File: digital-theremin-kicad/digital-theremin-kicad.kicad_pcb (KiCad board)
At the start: 2 copper layers, 99.1 x 91.1 mm, 40 parts, among them J1 PICO_DDS, J10 R_SPEAKER, J11 L_SPEAKER, J2 VL53L0X-VOL, J3 VL53L0X-FREQ, J4 ToDaughter1, J5 ToDaughter2, J6 Daughter1, J7 DISPLAY, J8 Daughter2, J9 PAM8403 module, SW1 SW_Push, SW2 SW_Push

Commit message: fixes for the digital circuit
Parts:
- moved J7 22.0 mm to (149.9, 123.1)
- moved R3 6.88 mm to (170.0, 91.0)
- moved H2 3.17 mm to (123.2, 140.3)
- moved H2 3.17 mm to (184.2, 140.3)
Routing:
- net +3V3: track 95.4 -> 114.7 mm
- net Net-(J6-Pin_3): track 30.4 -> 16.4 mm
- net GND: track 141.8 -> 132.1 mm
- net Net-(D1-A): track 11.8 -> 5.80 mm
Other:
- board size 99.1 x 91.1 mm -> 99.1 x 87.9 mm
- board text added: "3V3, GND, SCL, SDA"
- board text added: "Balaskó Tímea, Bodnár István, Borbély Sára, Briczky Balázs, Lajtos Hanna, Rácz Réka"
- board text removed: "Balaskó Tímea, Bodnár István, Borbély Sára, Bricky Balázs, Lajtos Hanna, Rácz Réka"

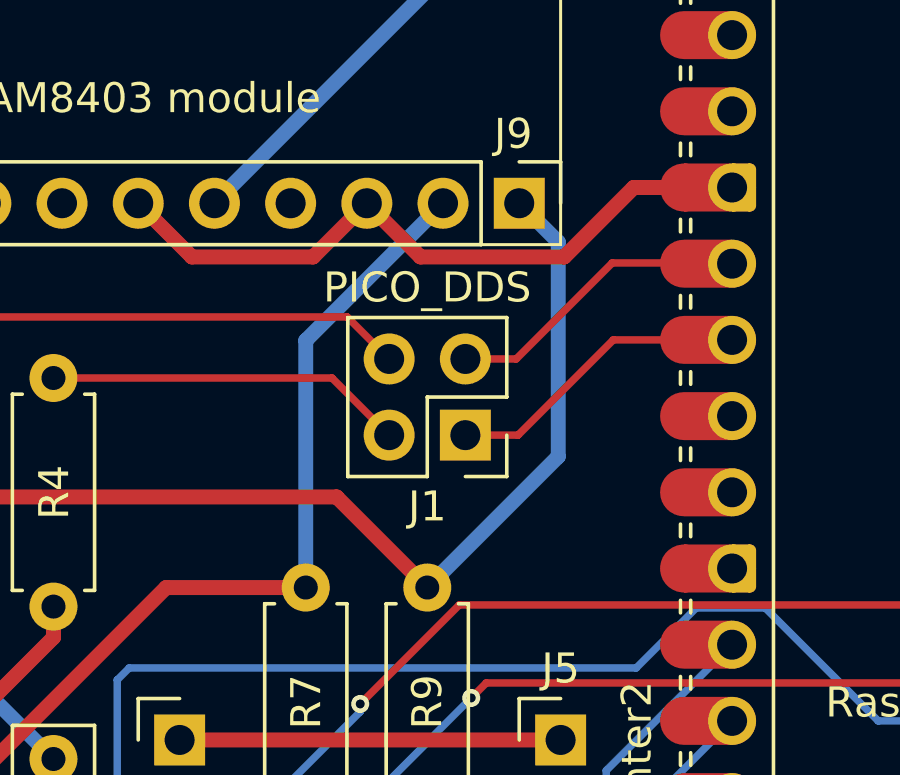
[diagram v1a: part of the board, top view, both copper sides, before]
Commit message: code for the digital theremin
- code is added for digital theremin
- minor fixes for the pcb
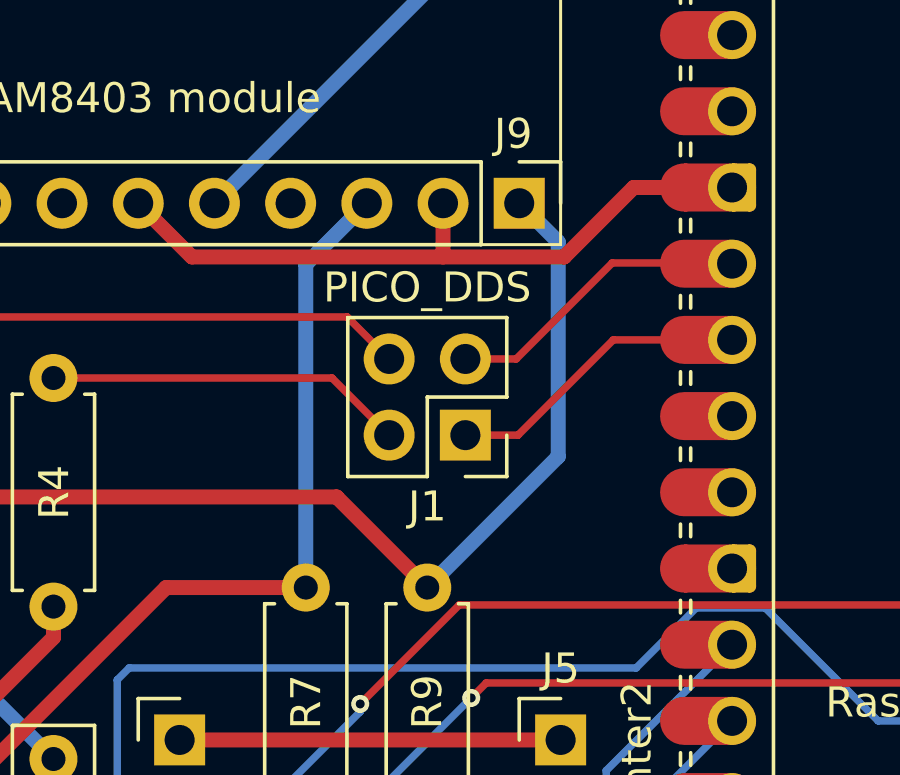
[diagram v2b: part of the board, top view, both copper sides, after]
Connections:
- J9 pad 2: Net-(J9-Pin_2) -> GND
- J9 pad 3: GND -> Net-(J9-Pin_3)
- R10 pad 2: Net-(J9-Pin_2) -> Net-(J9-Pin_3)
- R6 pad 2: Net-(J9-Pin_2) -> Net-(J9-Pin_3)
- R7 pad 2: Net-(J9-Pin_2) -> Net-(J9-Pin_3)
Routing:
- net Net-(J9-Pin_2): track 43.6 -> 0.00 mm
- net Net-(J9-Pin_3): track 0.00 -> 42.6 mm
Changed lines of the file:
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@@
 	(net 57 "Net-(C2-Pad1)")
 	(net 58 "Net-(C3-Pad1)")
-	(net 59 "Net-(J9-Pin_2)")
+	(net 59 "Net-(J9-Pin_3)")
 	(net 60 "Net-(J11-Pin_2)")
 	(footprint "LED_THT:LED_D5.0mm"
@@
 			(layers "*.Cu" "*.Mask")
 			(remove_unused_layers no)
-			(net 59 "Net-(J9-Pin_2)")
+			(net 59 "Net-(J9-Pin_3)")
 			(pintype "passive")
 		)
@@
 			(layers "*.Cu" "*.Mask")
 			(remove_unused_layers no)
-			(net 59 "Net-(J9-Pin_2)")
+			(net 3 "GND")
 			(pinfunction "Pin_2")
 			(pintype "passive")
@@
 			(layers "*.Cu" "*.Mask")
 			(remove_unused_layers no)
-			(net 3 "GND")
+			(net 59 "Net-(J9-Pin_3)")
 			(pinfunction "Pin_3")
 			(pintype "passive")
@@
 			(layers "*.Cu" "*.Mask")
 			(remove_unused_layers no)
-			(net 59 "Net-(J9-Pin_2)")
+			(net 59 "Net-(J9-Pin_3)")
 			(pintype "passive")
 		)
@@
 			(layers "*.Cu" "*.Mask")
 			(remove_unused_layers no)
-			(net 59 "Net-(J9-Pin_2)")
+			(net 59 "Net-(J9-Pin_3)")
 			(pintype "passive")
 		)
@@
 	)
 	(segment
+		(start 141.515 78.185)
+		(end 139.2 80.5)
+		(width 0.5)
+		(layer "F.Cu")
+		(net 3)
+	)
+	(segment
 		(start 122.175 102.235)
 		(end 118.125 102.235)
@@
 	)
 	(segment
+		(start 125 78.71)
+		(end 126.79 80.5)
+		(width 0.5)
+		(layer "F.Cu")
+		(net 3)
+	)
+	(segment
 		(start 139.08 99.14)
 		(end 143.525 103.585)
@@
 	)
 	(segment
-		(start 139.2 80.5)
-		(end 141.515 78.185)
-		(width 0.5)
-		(layer "F.Cu")
-		(net 3)
-	)
-	(segment
 		(start 165.9 102.85)
 		(end 165.165 103.585)
@@
 	)
 	(segment
-		(start 134.41 80.5)
+		(start 126.79 80.5)
 		(end 139.2 80.5)
 		(width 0.5)
@@
 	)
 	(segment
-		(start 126.79 80.5)
-		(end 130.83 80.5)
-		(width 0.5)
-		(layer "F.Cu")
-		(net 3)
-	)
-	(segment
-		(start 125 78.71)
-		(end 126.79 80.5)
-		(width 0.5)
-		(layer "F.Cu")
-		(net 3)
-	)
-	(segment
 		(start 168.29 99.14)
 		(end 168.16 99.14)
@@
 	)
 	(segment
-		(start 132.62 78.71)
-		(end 134.41 80.5)
-		(width 0.5)
-		(layer "F.Cu")
-		(net 3)
-	)
-	(segment
-		(start 130.83 80.5)
-		(end 132.62 78.71)
+		(start 125.27 99.14)
+		(end 122.175 102.235)
 		(width 0.5)
 		(layer "F.Cu")
@@
 	)
 	(segment
-		(start 125.27 99.14)
-		(end 122.175 102.235)
+		(start 143.995 78.185)
+		(end 141.515 78.185)
 		(width 0.5)
 		(layer "F.Cu")
@@
 	)
 	(segment
-		(start 141.515 78.185)
-		(end 143.995 78.185)
+		(start 165.165 103.585)
+		(end 163.375 103.585)
 		(width 0.5)
 		(layer "F.Cu")
@@
 	)
 	(segment
-		(start 165.165 103.585)
-		(end 163.375 103.585)
+		(start 135.16 80.5)
+		(end 135.16 78.71)
 		(width 0.5)
 		(layer "F.Cu")
@@
 	)
 	(segment
-		(start 130.585 83.285)
-		(end 135.16 78.71)
+		(start 130.585 91.52)
+		(end 130.585 80.745)
 		(width 0.5)
 		(layer "B.Cu")
@@
 	)
 	(segment
-		(start 130.585 91.52)
-		(end 130.585 83.285)
+		(start 130.585 80.745)
+		(end 132.62 78.71)
 		(width 0.5)
 		(layer "B.Cu")

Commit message: minor update to the pcb
minor update to the pcb
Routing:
- net +3V3: track 114.7 -> 191.7 mm
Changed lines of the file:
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@@
+	)
+	(segment
+		(start 124.46 97.028)
+		(end 124.46 97.79)
+		(width 0.5)
+		(layer "F.Cu")
+		(net 16)
+	)
+	(segment
+		(start 123.223 111.285)
+		(end 171.385 111.285)
+		(width 0.5)
+		(layer "F.Cu")
+		(net 16)
 	)
 	(segment
@@
 	)
 	(segment
+		(start 126.38 96.6)
+		(end 124.888 96.6)
+		(width 0.5)
+		(layer "F.Cu")
+		(net 16)
+	)
+	(segment
 		(start 168.29 92.71)
 		(end 168.29 96.6)
+		(width 0.5)
+		(layer "F.Cu")
+		(net 16)
+	)
+	(segment
+		(start 124.46 97.79)
+		(end 121.666 100.584)
 		(width 0.5)
 		(layer "F.Cu")
@@
 	)
 	(segment
+		(start 117.348 100.584)
+		(end 116.332 101.6)
+		(width 0.5)
+		(layer "F.Cu")
+		(net 16)
+	)
+	(segment
 		(start 182.41 96.6)
 		(end 186.5 100.69)
@@
 	)
 	(segment
+		(start 116.332 101.6)
+		(end 116.332 104.394)
+		(width 0.5)
+		(layer "F.Cu")
+		(net 16)
+	)
+	(segment
 		(start 126.38 96.6)
 		(end 139.08 96.6)
+		(width 0.5)
+		(layer "F.Cu")
+		(net 16)
+	)
+	(segment
+		(start 171.385 111.285)
+		(end 174.005 108.665)
+		(width 0.5)
+		(layer "F.Cu")
+		(net 16)
+	)
+	(segment
+		(start 116.332 104.394)
+		(end 123.223 111.285)
 		(width 0.5)
 		(layer "F.Cu")
@@
 	)
 	(segment
+		(start 124.888 96.6)
+		(end 124.46 97.028)
+		(width 0.5)
+		(layer "F.Cu")
+		(net 16)
+	)
+	(segment
 		(start 175.39 91)
 		(end 180.99 96.6)
 		(width 0.5)
 		(layer "F.Cu")
+		(net 16)
+	)
+	(segment
+		(start 121.666 100.584)
+		(end 117.348 100.584)
+		(width 0.5)
+		(layer "F.Cu")
